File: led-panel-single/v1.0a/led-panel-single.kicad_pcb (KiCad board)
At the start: 2 copper layers, 42 x 20 mm, 22 parts, among them J1 5V, J2 jmp, J3 Conn_02x08_Odd_Even, J4 PMOD, J5 jmp, U1 SN74LVC8T245, U2 NL27WZ14, U3 74HC4024, U4 74VHC574

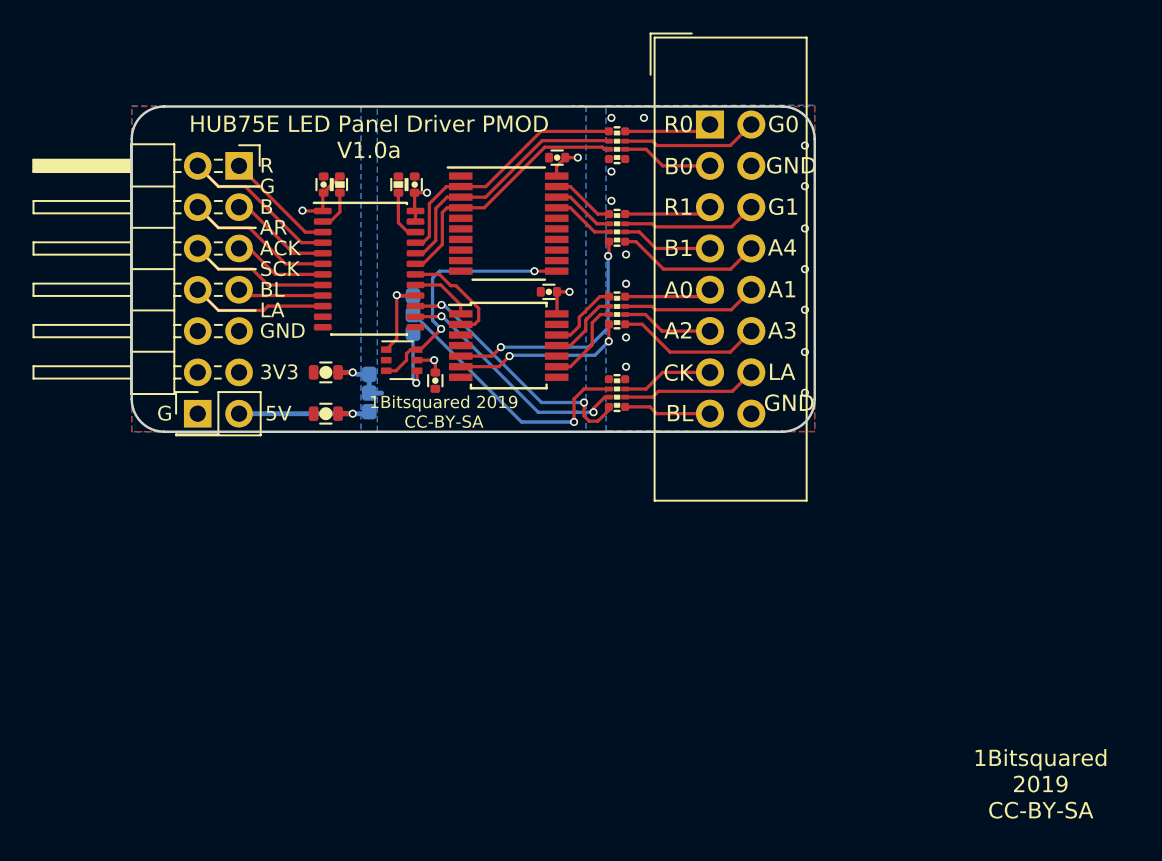
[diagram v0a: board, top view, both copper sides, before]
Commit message: Optimized layout and shortened the board by 2mm.
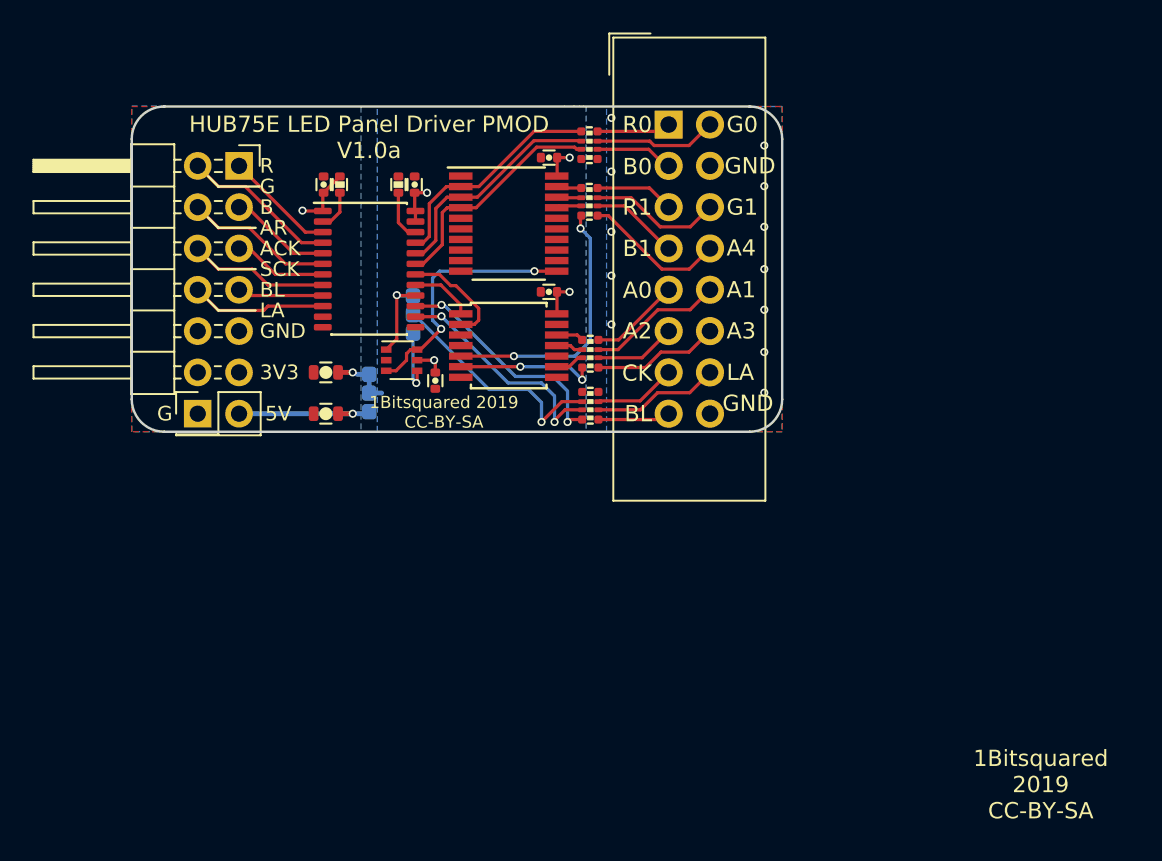
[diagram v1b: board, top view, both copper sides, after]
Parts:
- moved R2 3.13 mm to (65.6, 49.2)
- moved J3 2.54 mm to (70.4, 35.1)
- moved R6 2.33 mm to (65.5, 39.9)
- moved R4 1.82 mm to (65.6, 52.4)
- moved R5 1.70 mm to (65.5, 36.4)
- moved C6 0.50 mm to (63.1, 37.1)
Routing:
- net /A2: track 5.33 -> 1.79 mm
- net /A1: track 4.57 -> 1.67 mm
- net /A0: track 4.51 -> 1.69 mm
- net /G1: track 3.89 -> 1.53 mm
- net /R1: track 3.91 -> 1.55 mm
- net /B1: track 3.83 -> 1.56 mm
- net /A3: track 10.8 -> 8.63 mm
- net /SCLKi: track 16.5 -> 14.4 mm
- net /B: track 16.1 -> 14.4 mm
- net /R: track 15.9 -> 14.2 mm
- net /G: track 15.9 -> 14.3 mm
- net /BLANK: track 15.9 -> 14.4 mm
- net /A4: track 15.1 -> 16.3 mm
- net /A3x: track 9.00 -> 7.79 mm
- net /BLANKx: track 5.39 -> 4.47 mm
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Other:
- board size 42 x 20 mm -> 40 x 20 mm

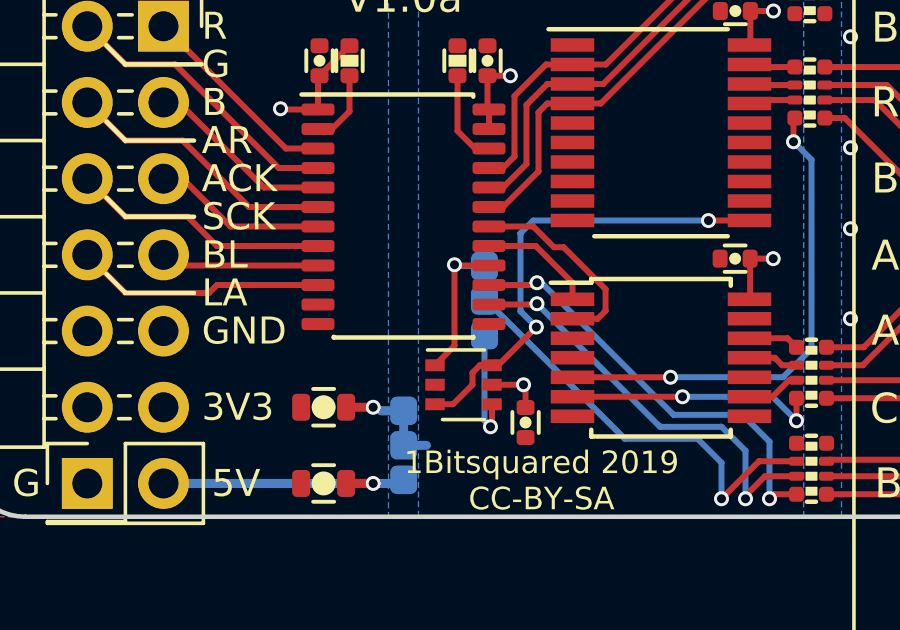
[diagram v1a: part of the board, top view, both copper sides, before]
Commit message: Rerouted SCLK to improve level shifter ground connection.
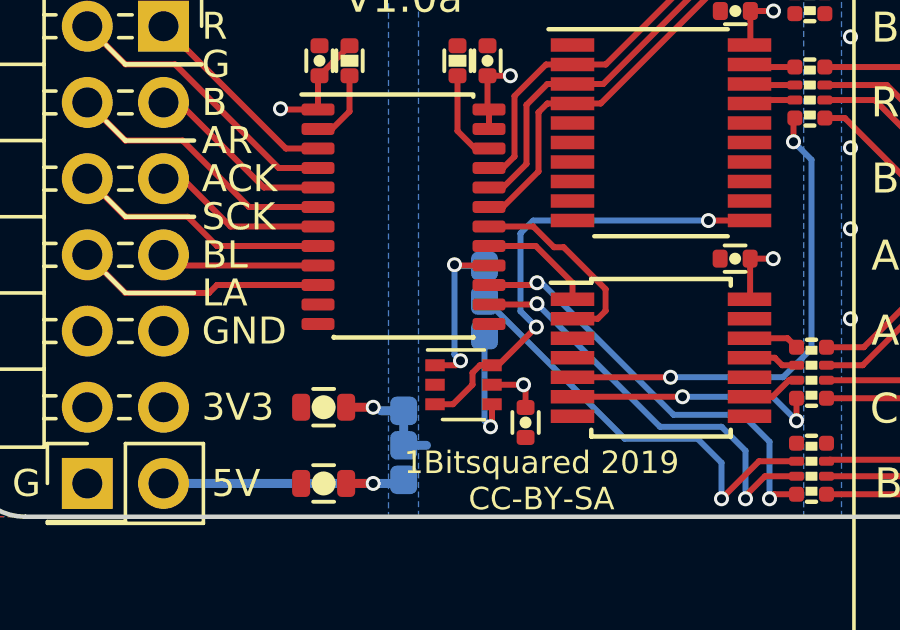
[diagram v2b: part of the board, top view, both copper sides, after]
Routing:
- net /SCLK: track 6.26 -> 6.80 mm, vias 1 -> 2
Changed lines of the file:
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@@
     (thickness 0.8)
     (drawings 95)
-    (tracks 251)
+    (tracks 253)
     (zones 0)
     (modules 22)
@@
   (segment (start 54.85 45.625) (end 54.384298 45.625) (width 0.2) (layer F.Cu) (net 25))
   (via (at 53.699994 45.6) (size 0.5) (drill 0.3) (layers F.Cu B.Cu) (net 25))
-  (segment (start 53.724994 45.625) (end 53.699994 45.6) (width 0.2) (layer F.Cu) (net 25))
   (segment (start 54.85 45.625) (end 53.724994 45.625) (width 0.2) (layer F.Cu) (net 25))
-  (segment (start 53.699994 48.300006) (end 53.699994 45.6) (width 0.2) (layer F.Cu) (net 25))
-  (segment (start 53.05 48.95) (end 53.699994 48.300006) (width 0.2) (layer F.Cu) (net 25))
   (segment (start 53.743994 45.644) (end 53.699994 45.6) (width 0.2) (layer B.Cu) (net 25))
   (segment (start 54.7 45.644) (end 53.743994 45.644) (width 0.2) (layer B.Cu) (net 25))
+  (via (at 53.9 48.8) (size 0.5) (drill 0.3) (layers F.Cu B.Cu) (net 25))
+  (segment (start 53.699994 45.6) (end 53.699994 48.599994) (width 0.2) (layer B.Cu) (net 25))
+  (segment (start 53.699994 48.599994) (end 53.9 48.8) (width 0.2) (layer B.Cu) (net 25))
+  (segment (start 53.75 48.95) (end 53.9 48.8) (width 0.2) (layer F.Cu) (net 25))
+  (segment (start 53.05 48.95) (end 53.75 48.95) (width 0.2) (layer F.Cu) (net 25))
   (segment (start 56.42501 46.925) (end 56.45001 46.9) (width 0.2) (layer F.Cu) (net 26))
   (via (at 56.45001 46.9) (size 0.5) (drill 0.3) (layers F.Cu B.Cu) (net 26))

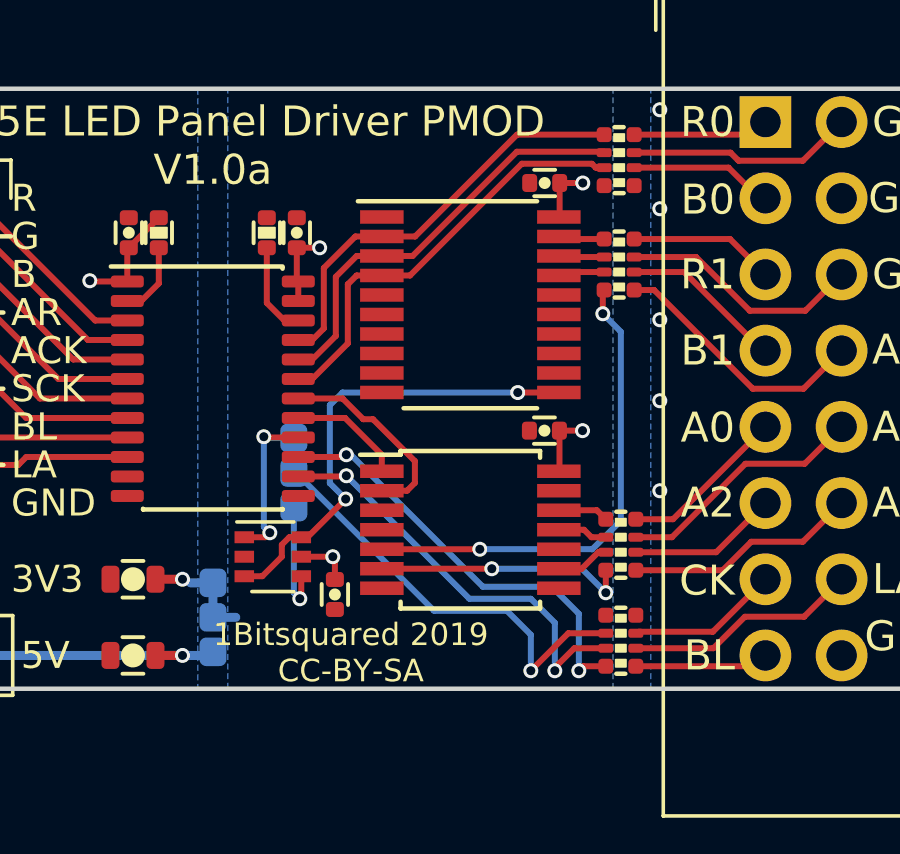
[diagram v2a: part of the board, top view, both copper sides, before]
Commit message: Corrected TSSOP footprints to make them consistent.
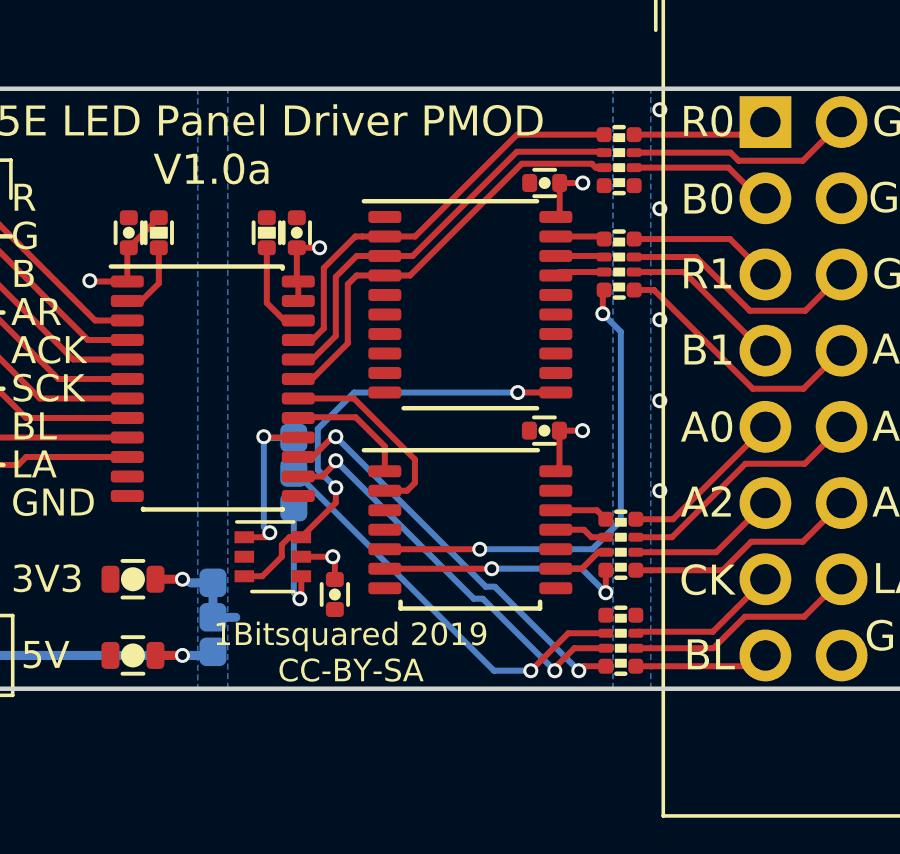
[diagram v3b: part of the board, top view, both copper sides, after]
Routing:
- net /SCLKi: track 14.4 -> 13.7 mm
- net /BLANK: track 14.4 -> 13.8 mm
